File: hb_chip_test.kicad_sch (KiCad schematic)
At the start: 158 parts, among them J1 31-5431-2010_CID2.5.196, J2 31-5431-2010_CID2.5.196, J3 31-5431-2010_CID2.5.196, J4 1945193_12P_CID2.2.928, J5 31-5431-2010_CID2.5.196, J6 31-5431-2010_CID2.5.196, J7 31-5431-2010_CID2.5.196, U1 L7812ABD2T-TR_CID8.52.934, U2 MC7912ACD2TR4G_CID8.52.429, U3 LP2981IM5-5.0-NOPB_CID8.52.176, U5 TL084, U6 MCP3202, U7 REF5050ID, U8 Tang_Nano_9K, U9 TL082

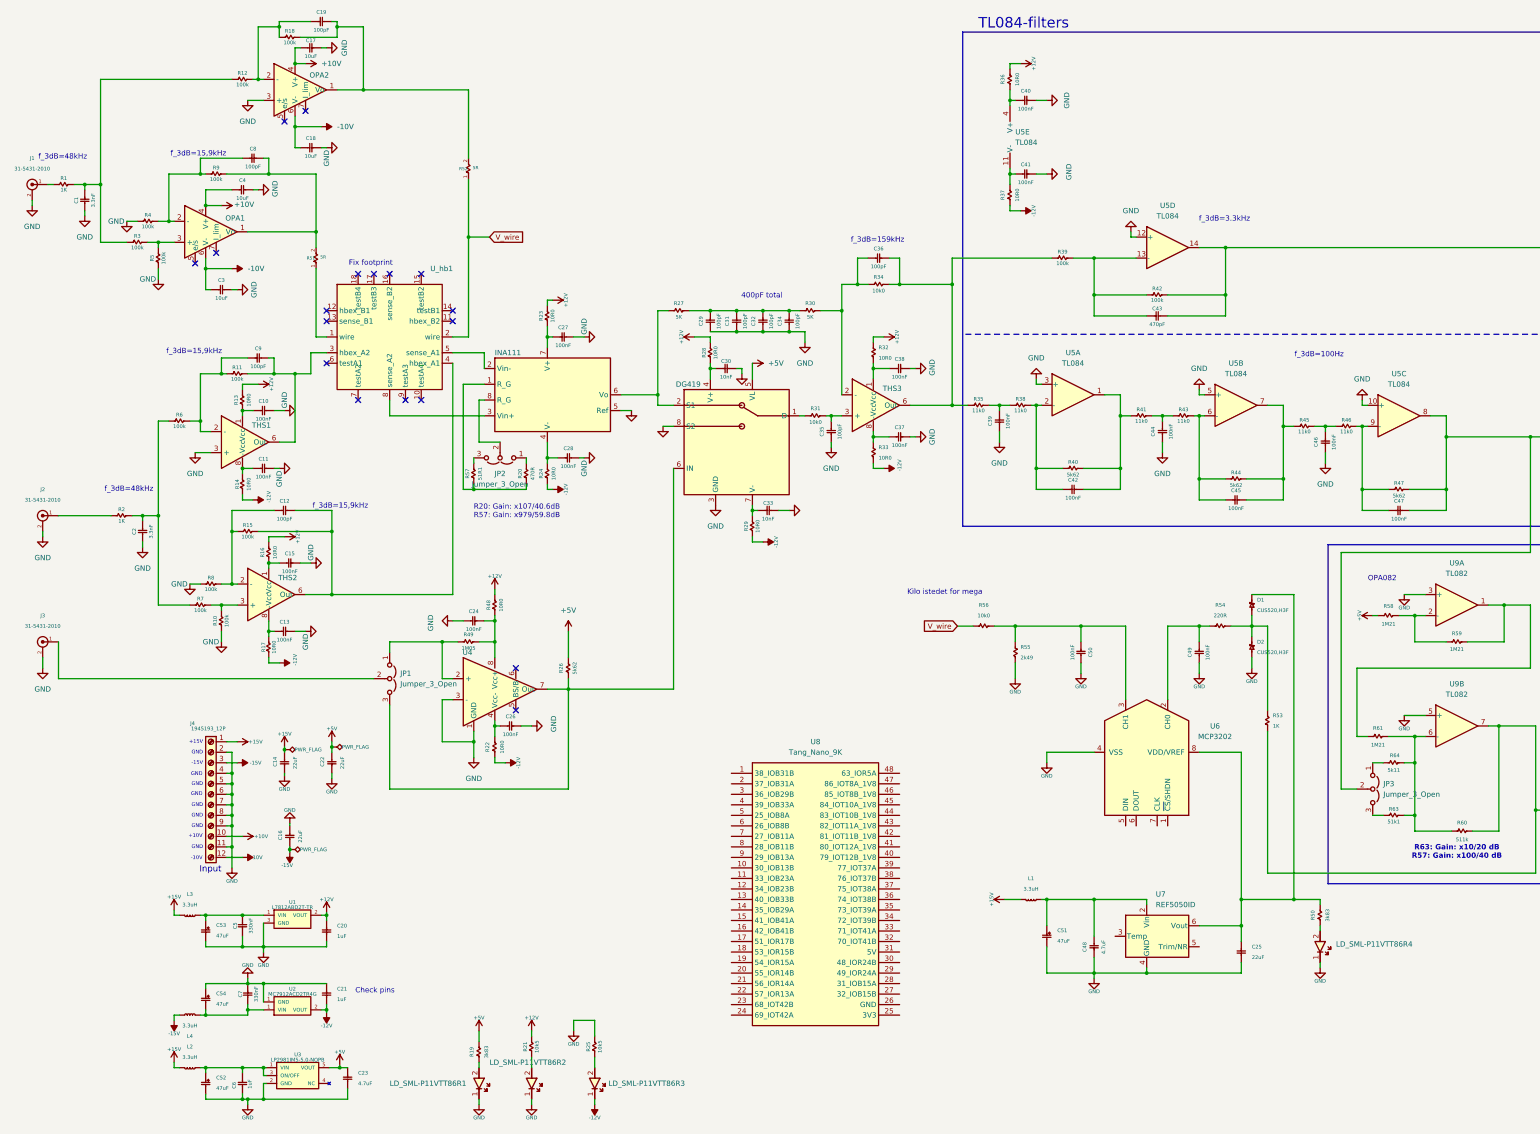
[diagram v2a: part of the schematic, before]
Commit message: HB driver jumpers + PCBv1
TangNano9k has been wired.

Jumpers place for the hb drive but no bnc's for this. If something else is to drive it it can be done from jumpers.

PCB is in the layout v1 now. Still missing socket for the chip.
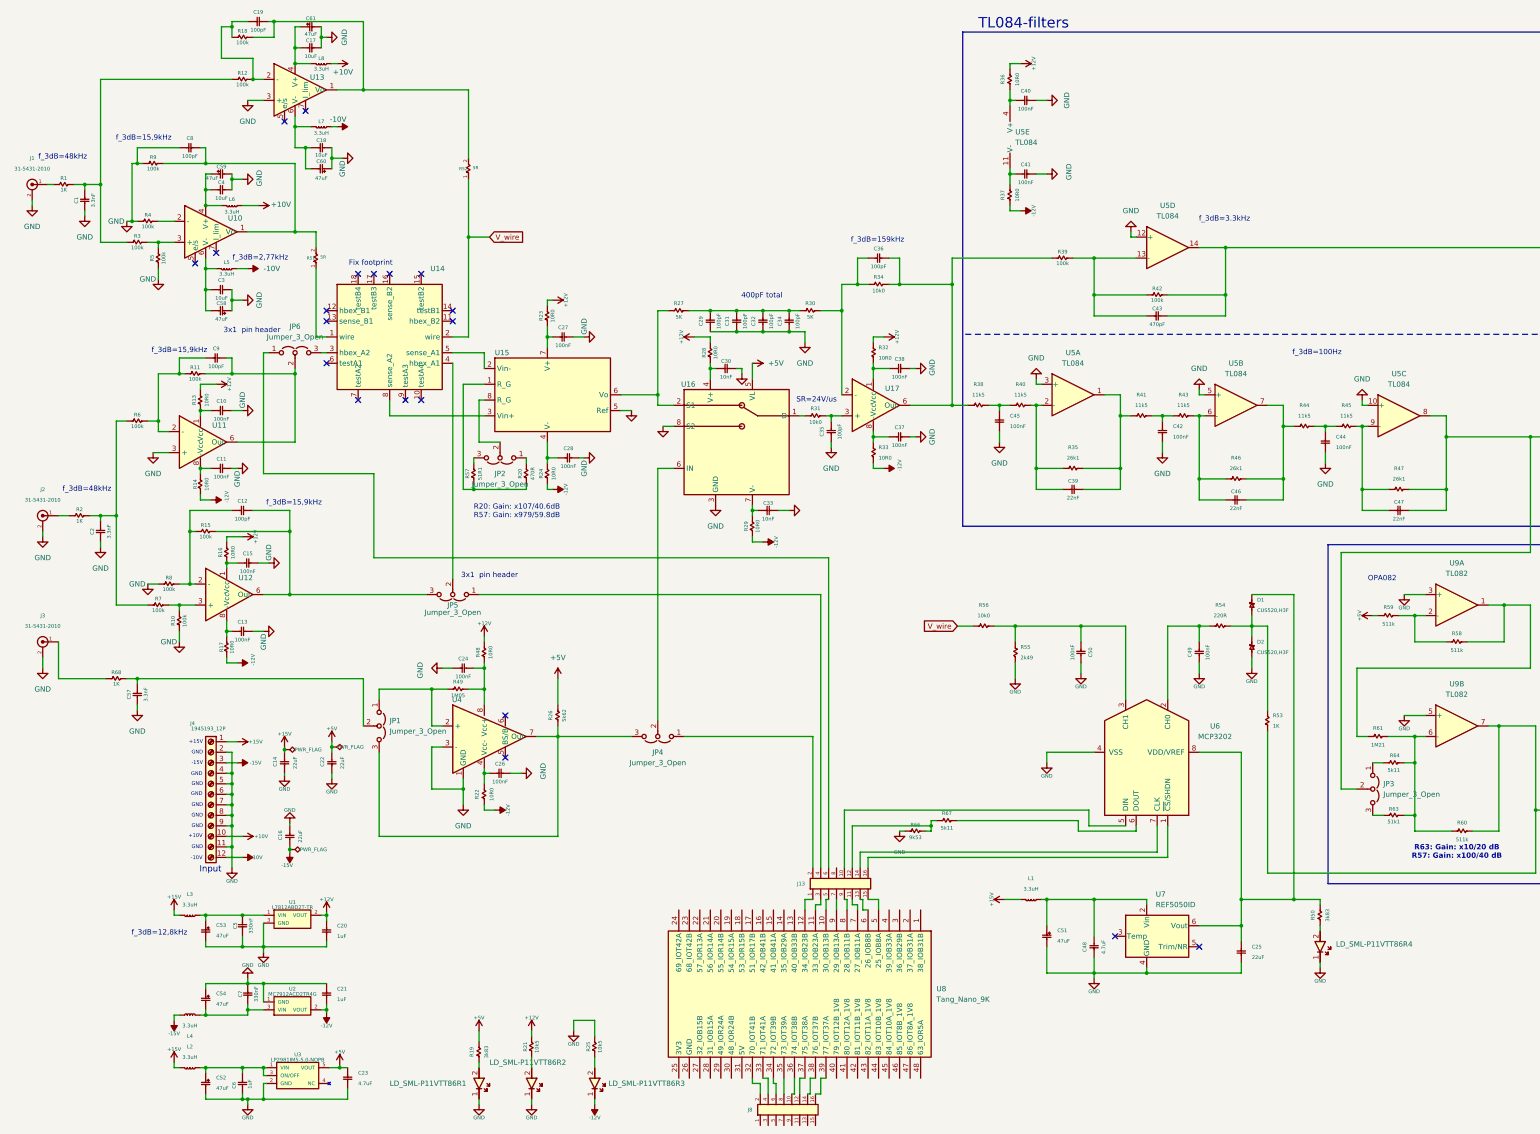
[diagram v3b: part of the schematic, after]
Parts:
- removed C39, C46, C47: C_0805_100nF_16V_X7R_CID1.2.3078, C0805_CAPC200X125X130L45N, symbol 1-Capacitor:C_0805_100nF_16V_X7R_CID1.2.3078
- removed R35, R38, R41, R43, R45, R46: R_0805_11k0_CID10.9.5869, R0805_RESC200X125X50L35N, symbol 10-Resistor:R_0805_11k0_CID10.9.5869
- removed R40, R44, R47: R_0805_5k62_CID10.9.159, R0805_RESC200X125X50L35N, symbol 10-Resistor:R_0805_5k62_CID10.9.159
- removed R58, R59: R_0805_1M21_CID10.9.5950, R0805_RESC200X125X50L35N, symbol 10-Resistor:R_0805_1M21_CID10.9.5950
- added C39, C46, C47: C_0402_22nF_16V_X7R_CID1.2.2613, C0402_CAPC100X50X61L25N, symbol 1-Capacitor:C_0402_22nF_16V_X7R_CID1.2.2613
- added C57: C_0402_3.3nF_16V_X7R_CID1.2.2599, C0402_CAPC100X50X61L25N, symbol 1-Capacitor:C_0402_3.3nF_16V_X7R_CID1.2.2599
- added C58, C59, C60, C61: C_2917_47uF_20V_20%_CID1.3.892, dtuspace_ipc:C2917_CAPC730X430X310L130N, symbol 1-Capacitor:C_2917_47uF_20V_20%_CID1.3.892
- added J13, J8: 2x8, dtuspace_ipc:HEADER-P254-2x8, symbol 2-Connectors:SFH11-PBPC-D08-ST-BK_CID2.2.662
- added JP4, JP5, JP6: Jumper_3_Open, dtuspace_ipc:HEADER-P254-1x3, symbol Jumper:Jumper_3_Open
- added L5, L6, L7, L8: L_3.3uH_870mA_CID7.3.944, L0805_INDC200X125X140L50N, symbol 7-Inductor:L_3.3uH_870mA_CID7.3.944
- added R35, R46, R47: R_0805_26k1_CID10.9.5881, R0805_RESC200X125X50L35N, symbol 10-Resistor:R_0805_26k1_CID10.9.5881
- added R38, R40, R41, R43, R44, R45: R_0805_11k5_CID10.9.5870, R0805_RESC200X125X50L35N, symbol 10-Resistor:R_0805_11k5_CID10.9.5870
- added R58, R59: R_0805_511k_CID10.9.489, R0805_RESC200X125X50L35N, symbol 10-Resistor:R_0805_511k_CID10.9.489
- added R66: R_0805_9k53_CID10.9.5867, R0805_RESC200X125X50L35N, symbol 10-Resistor:R_0805_9k53_CID10.9.5867
- added R67: R_0805_5k11_CID10.9.467, R0805_RESC200X125X50L35N, symbol 10-Resistor:R_0805_5k11_CID10.9.467
- added R68: R_0805_1K_CID10.99.611, R0805_RESC200X125X50L35N, symbol 10-Resistor:R_0805_1K_CID10.99.611
- D1, D2: footprint dtuspace:SOD250X130X120L30X30N -> dtuspace_ipc:SOD250X130X120L30X30N
- JP1, JP2, JP3: footprint dtuspace_ipc:2_WAY_SOLDER_JUMPER -> dtuspace_ipc:HEADER-P254-1x3
- U9: footprint (none) -> dtuspace_ipc:SOIC8P127_490X600X175L83X41N
- renumbered OPA1 to U10, THS1 to U11, THS2 to U12, OPA2 to U13, U_hb1 to U14, INA111 to U15, DG419 to U16, THS3 to U17
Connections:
- net +10V: now also L6.2, L8.2; no longer C17.1, C4.1, U10.4 (V+), U13.4 (V+)
- net +5V: now also R59.1
- net -10V: now also L5.2, L7.2; no longer C18.1, C3.1, U10.6 (V-), U13.6 (V-)
- net GND: now also C42.2, C44.2, C45.2, C8.1, R9.1, C57.1, C58.1, C59.2, C60.1, C61.2, R66.1; no longer C44.1
- net at C9.2, R11.2, U11.6 (Out): now also JP6.2 (C); no longer U14.3 (hbex_A2)
- net at JP1.3 (B), R26.1, U4.7 (Out): now also JP4.3 (B); no longer U16.6 (IN)
- net at C42.1: now also R41.2, R43.1; no longer U5.2 (-)
- net at C36.2, R34.2, R39.1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: now also R38.1
- net at J5.1, JP3.2 (C), U5.8: now also C47.2, R47.2
- net at U5.1: now also C39.2, R35.2, R41.1; no longer C42.2
- net at R4.2, U10.2 (-): no longer C8.1, R9.1
- net at U5.9 (-): now also C47.1, R45.2, R47.1
- net at C54.2, C7.1, L4.2: now also U2.3 (VIN); no longer U2.1 (VIN)
- net at U5.6 (-): now also C46.1, R43.2, R46.1; no longer C45.1
- net at U5.7: now also C46.2, R44.1, R46.2; no longer C45.2
- net at C12.2, R15.2, U12.6 (Out): now also JP5.3 (B); no longer U14.4 (hbex_A1)
- net at U9.2 (-): now also R58.1, R59.2
- net at R61.1, U9.1: now also R58.2
- net at U8.10 (30_IOB13B): now also J13.5
- net at U8.11 (33_IOB23A): now also J13.3
- net at U8.12 (34_IOB23B): now also J13.1
- net at U8.32 (70_IOT41B): now also J8.2
- net at U8.33 (71_IOT41A): now also J8.4
- net at U8.34 (72_IOT39B): now also J8.6
- net at U8.35 (73_IOT39A): now also J8.8
- net at U8.36 (74_IOT38B): now also J8.10
- net at U8.37 (75_IOT38A): now also J8.12
- net at U8.38 (76_IOT37B): now also J8.14
- net at U8.39 (77_IOT37A): now also J8.16
- net at U8.5 (25_IOB8A): now also J13.15
- net at U8.6 (26_IOB8B): now also J13.13
- net at U8.7 (27_IOB11A): now also J13.11
- net at U8.8 (28_IOB11B): now also J13.9
- net at U8.9 (29_IOB13A): now also J13.7
- net at JP1.2 (C): now also C57.2, R68.2; no longer J3.1
- net at U6.1 (~{CS}/SHDN): now also J13.16
- net at U6.5 (DIN): now also J13.10
- net at U6.6 (DOUT): now also R67.2
- net at U6.7 (CLK): now also J13.14
- new net: C45.1, R38.2, R40.1
- new net: J13.12, R66.2, R67.1
- new net: J13.2, JP4.1 (A)
- new net: J13.4, JP5.1 (A)
- new net: J13.6, JP6.1 (A)
- new net: JP6.3 (B), U14.3 (hbex_A2)
- new net: C4.1, C59.1, L6.1, U10.4 (V+)
- new net: C3.1, C58.2, L5.1, U10.6 (V-)
- new net: C17.1, C61.1, L8.1, U13.4 (V+)
- new net: C39.1, R35.1, R40.2, U5.2 (-)
- new net: C44.1, R44.2, R45.1
- new net: JP4.2 (C), U16.6 (IN)
- new net: JP5.2 (C), U14.4 (hbex_A1)
- new net: J3.1, R68.1
- new net: C18.1, C60.2, L7.1, U13.6 (V-)
- no-connect marks 18 -> 20
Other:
- note added: "3x1 pin header"
- note added: "SR=24V/us"
- note added: "f_3dB=12,8kHz"
- note added: "f_3dB=2,77kHz"
- note removed: "Check pins"
- note removed: "Kilo istedet for mega"
- moved on the sheet: C10, C11, C12, C13, C15, C18, C19, C2, C24, C26, C4, C8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
